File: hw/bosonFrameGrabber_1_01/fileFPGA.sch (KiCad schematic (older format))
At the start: 16 parts, among them U3 ICE40HX8K, X1 ASDMB

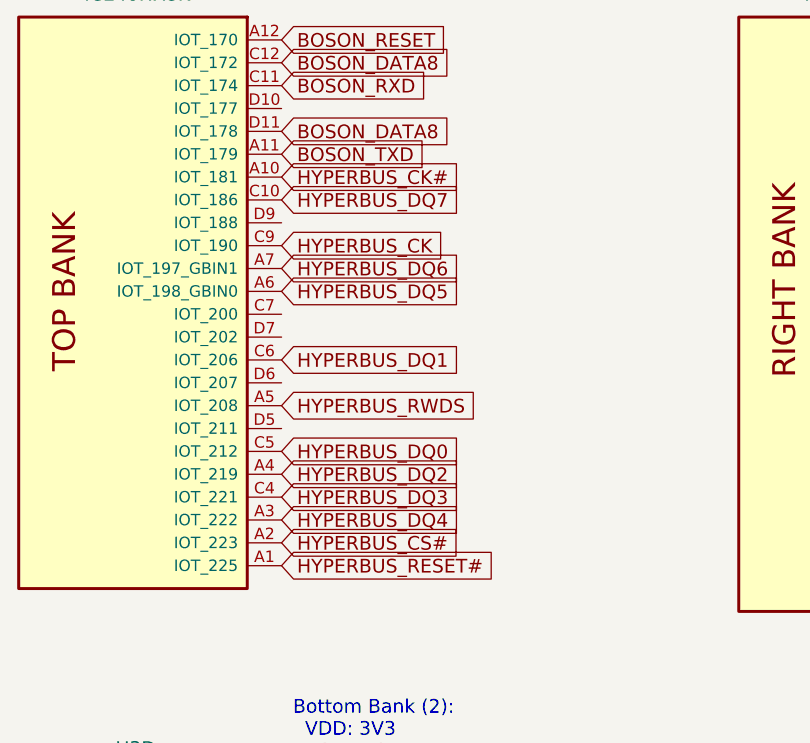
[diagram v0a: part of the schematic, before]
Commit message: Updates to project documentation.
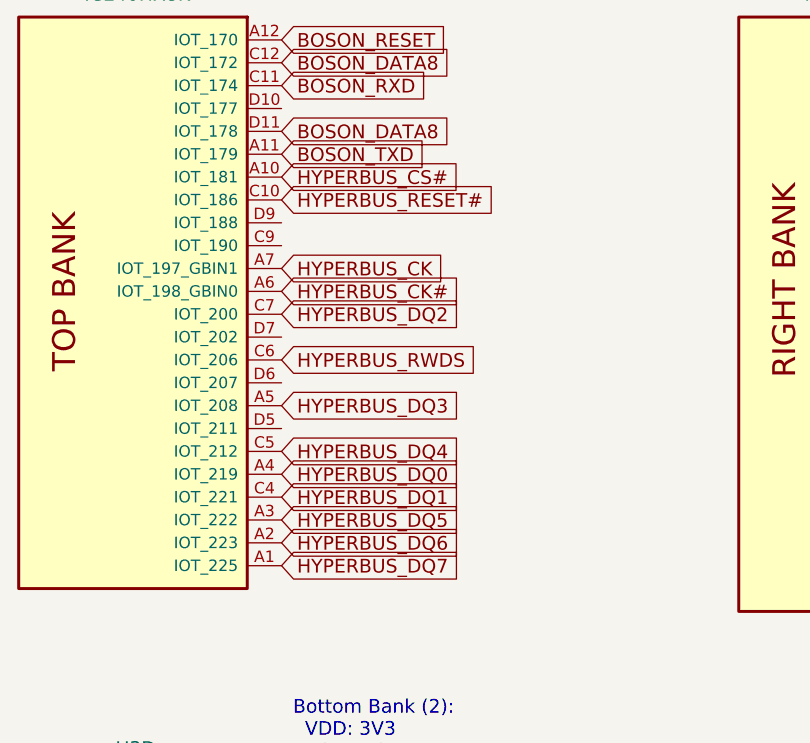
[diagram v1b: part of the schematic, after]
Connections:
- net HYPERBUS_CK: now also U3.A7 (IOT_197_GBIN1); no longer U3.C9 (IOT_190)
- net HYPERBUS_CK#: now also U3.A6 (IOT_198_GBIN0); no longer U3.A10 (IOT_181)
- net HYPERBUS_CS#: now also U3.A10 (IOT_181); no longer U3.A2 (IOT_223)
- net HYPERBUS_DQ0: now also U3.A4 (IOT_219); no longer U3.C5 (IOT_212)
- net HYPERBUS_DQ1: now also U3.C4 (IOT_221); no longer U3.C6 (IOT_206)
- net HYPERBUS_DQ2: now also U3.C7 (IOT_200); no longer U3.A4 (IOT_219)
- net HYPERBUS_DQ3: now also U3.A5 (IOT_208); no longer U3.C4 (IOT_221)
- net HYPERBUS_DQ4: now also U3.C5 (IOT_212); no longer U3.A3 (IOT_222)
- net HYPERBUS_DQ5: now also U3.A3 (IOT_222); no longer U3.A6 (IOT_198_GBIN0)
- net HYPERBUS_DQ6: now also U3.A2 (IOT_223); no longer U3.A7 (IOT_197_GBIN1)
- net HYPERBUS_DQ7: now also U3.A1 (IOT_225); no longer U3.C10 (IOT_186)
- net HYPERBUS_RESET#: now also U3.C10 (IOT_186); no longer U3.A1 (IOT_225)
- net HYPERBUS_RWDS: now also U3.C6 (IOT_206); no longer U3.A5 (IOT_208)
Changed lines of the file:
@@
 Text GLabel 2450 5800 2    60   Input ~ 0
 SD_CD
+Text GLabel 2450 3000 2    60   Input ~ 0
+HYPERBUS_RWDS
+Text GLabel 2450 2200 2    60   Input ~ 0
+HYPERBUS_CS#
+Text GLabel 2450 2300 2    60   Input ~ 0
+HYPERBUS_RESET#
+Text GLabel 2450 2600 2    60   Input ~ 0
+HYPERBUS_CK
+Text GLabel 2450 2700 2    60   Input ~ 0
+HYPERBUS_CK#
+Text GLabel 2450 3500 2    60   Input ~ 0
+HYPERBUS_DQ0
+Text GLabel 2450 3600 2    60   Input ~ 0
+HYPERBUS_DQ1
+Text GLabel 2450 2800 2    60   Input ~ 0
+HYPERBUS_DQ2
 Text GLabel 2450 3200 2    60   Input ~ 0
-HYPERBUS_RWDS
+HYPERBUS_DQ3
+Text GLabel 2450 3400 2    60   Input ~ 0
+HYPERBUS_DQ4
+Text GLabel 2450 3700 2    60   Input ~ 0
+HYPERBUS_DQ5
 Text GLabel 2450 3800 2    60   Input ~ 0
-HYPERBUS_CS#
+HYPERBUS_DQ6
 Text GLabel 2450 3900 2    60   Input ~ 0
-HYPERBUS_RESET#
-Text GLabel 2450 2500 2    60   Input ~ 0
-HYPERBUS_CK
-Text GLabel 2450 2200 2    60   Input ~ 0
-HYPERBUS_CK#
-Text GLabel 2450 3400 2    60   Input ~ 0
-HYPERBUS_DQ0
-Text GLabel 2450 3000 2    60   Input ~ 0
-HYPERBUS_DQ1
-Text GLabel 2450 3500 2    60   Input ~ 0
-HYPERBUS_DQ2
-Text GLabel 2450 3600 2    60   Input ~ 0
-HYPERBUS_DQ3
-Text GLabel 2450 3700 2    60   Input ~ 0
-HYPERBUS_DQ4
-Text GLabel 2450 2700 2    60   Input ~ 0
-HYPERBUS_DQ5
-Text GLabel 2450 2600 2    60   Input ~ 0
-HYPERBUS_DQ6
-Text GLabel 2450 2300 2    60   Input ~ 0
 HYPERBUS_DQ7
 Text GLabel 5600 1900 2    60   Input ~ 0
